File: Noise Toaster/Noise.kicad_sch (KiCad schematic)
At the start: 11 parts, among them Q5 2N3904, Q6 2N3904, Q7 2N3904

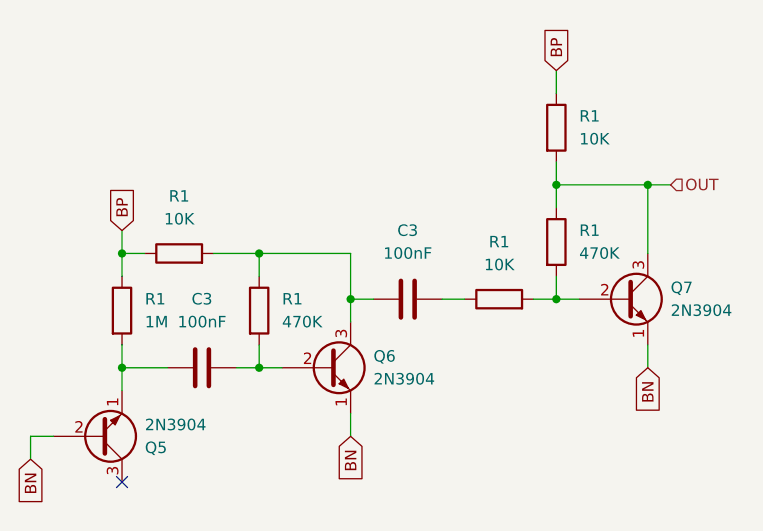
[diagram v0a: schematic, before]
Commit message: Noise Toaster - fixes after first board
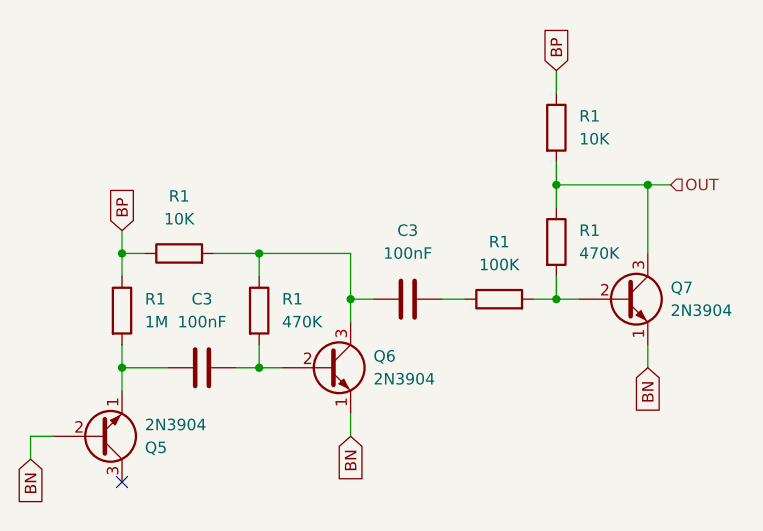
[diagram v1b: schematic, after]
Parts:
- R1: value 10K -> 100K
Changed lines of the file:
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@@
       (effects (font (size 1.27 1.27)))
     )
-    (property "Value" "10K" (at 160.02 92.71 90)
+    (property "Value" "100K" (at 160.02 92.71 90)
       (effects (font (size 1.27 1.27)))
     )

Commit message: misc
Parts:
- renumbered C3 to C15, C3 to C16, R1 to R33, R1 to R34, R1 to R35, R1 to R36, R1 to R37, R1 to R38
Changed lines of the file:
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@@
   (symbol (lib_id "Device:C") (at 149.86 96.52 270) (unit 1)
     (in_bom yes) (on_board yes) (dnp no) (fields_autoplaced)
-    (property "Reference" "C3" (at 149.86 88.9 90)
+    (property "Reference" "C16" (at 149.86 88.9 90)
       (effects (font (size 1.27 1.27)))
     )
@@
     (instances
       (project "Noise Toaster"
-        (path "/c06bdaff-9d92-4322-9a29-784b2d9ec2c6/3f36173e-f191-4036-853e-444de7299fbe"
-          (reference "C3") (unit 1)
-        )
         (path "/c06bdaff-9d92-4322-9a29-784b2d9ec2c6/059c9cca-6c24-4c13-86e8-c51a7e9129a9"
           (reference "C16") (unit 1)
@@
   (symbol (lib_id "Device:R") (at 118.11 97.79 0) (unit 1)
     (in_bom yes) (on_board yes) (dnp no) (fields_autoplaced)
-    (property "Reference" "R1" (at 120.65 96.52 0)
+    (property "Reference" "R33" (at 120.65 96.52 0)
       (effects (font (size 1.27 1.27)) (justify left))
     )
@@
     (instances
       (project "Noise Toaster"
-        (path "/c06bdaff-9d92-4322-9a29-784b2d9ec2c6/3f36173e-f191-4036-853e-444de7299fbe"
-          (reference "R1") (unit 1)
-        )
         (path "/c06bdaff-9d92-4322-9a29-784b2d9ec2c6/059c9cca-6c24-4c13-86e8-c51a7e9129a9"
           (reference "R33") (unit 1)
@@
   (symbol (lib_id "Device:R") (at 124.46 91.44 90) (unit 1)
     (in_bom yes) (on_board yes) (dnp no) (fields_autoplaced)
-    (property "Reference" "R1" (at 124.46 85.09 90)
+    (property "Reference" "R34" (at 124.46 85.09 90)
       (effects (font (size 1.27 1.27)))
     )
@@
     (instances
       (project "Noise Toaster"
-        (path "/c06bdaff-9d92-4322-9a29-784b2d9ec2c6/3f36173e-f191-4036-853e-444de7299fbe"
-          (reference "R1") (unit 1)
-        )
         (path "/c06bdaff-9d92-4322-9a29-784b2d9ec2c6/059c9cca-6c24-4c13-86e8-c51a7e9129a9"
           (reference "R34") (unit 1)
@@
   (symbol (lib_id "Device:R") (at 160.02 96.52 90) (unit 1)
     (in_bom yes) (on_board yes) (dnp no) (fields_autoplaced)
-    (property "Reference" "R1" (at 160.02 90.17 90)
+    (property "Reference" "R36" (at 160.02 90.17 90)
       (effects (font (size 1.27 1.27)))
     )
@@
     (instances
       (project "Noise Toaster"
-        (path "/c06bdaff-9d92-4322-9a29-784b2d9ec2c6/3f36173e-f191-4036-853e-444de7299fbe"
-          (reference "R1") (unit 1)
-        )
         (path "/c06bdaff-9d92-4322-9a29-784b2d9ec2c6/059c9cca-6c24-4c13-86e8-c51a7e9129a9"
           (reference "R36") (unit 1)
@@
   (symbol (lib_id "Device:R") (at 166.37 77.47 0) (unit 1)
     (in_bom yes) (on_board yes) (dnp no) (fields_autoplaced)
-    (property "Reference" "R1" (at 168.91 76.2 0)
+    (property "Reference" "R37" (at 168.91 76.2 0)
       (effects (font (size 1.27 1.27)) (justify left))
     )
@@
     (instances
       (project "Noise Toaster"
-        (path "/c06bdaff-9d92-4322-9a29-784b2d9ec2c6/3f36173e-f191-4036-853e-444de7299fbe"
-          (reference "R1") (unit 1)
-        )
         (path "/c06bdaff-9d92-4322-9a29-784b2d9ec2c6/059c9cca-6c24-4c13-86e8-c51a7e9129a9"
           (reference "R37") (unit 1)
@@
   (symbol (lib_id "Device:R") (at 133.35 97.79 0) (unit 1)
     (in_bom yes) (on_board yes) (dnp no) (fields_autoplaced)
-    (property "Reference" "R1" (at 135.89 96.52 0)
+    (property "Reference" "R35" (at 135.89 96.52 0)
       (effects (font (size 1.27 1.27)) (justify left))
     )
@@
     (instances
       (project "Noise Toaster"
-        (path "/c06bdaff-9d92-4322-9a29-784b2d9ec2c6/3f36173e-f191-4036-853e-444de7299fbe"
-          (reference "R1") (unit 1)
-        )
         (path "/c06bdaff-9d92-4322-9a29-784b2d9ec2c6/059c9cca-6c24-4c13-86e8-c51a7e9129a9"
           (reference "R35") (unit 1)
@@
   (symbol (lib_id "Device:C") (at 127 104.14 270) (unit 1)
     (in_bom yes) (on_board yes) (dnp no) (fields_autoplaced)
-    (property "Reference" "C3" (at 127 96.52 90)
+    (property "Reference" "C15" (at 127 96.52 90)
       (effects (font (size 1.27 1.27)))
     )
@@
     (instances
       (project "Noise Toaster"
-        (path "/c06bdaff-9d92-4322-9a29-784b2d9ec2c6/3f36173e-f191-4036-853e-444de7299fbe"
-          (reference "C3") (unit 1)
-        )
         (path "/c06bdaff-9d92-4322-9a29-784b2d9ec2c6/059c9cca-6c24-4c13-86e8-c51a7e9129a9"
           (reference "C15") (unit 1)
@@
   (symbol (lib_id "Device:R") (at 166.37 90.17 0) (unit 1)
     (in_bom yes) (on_board yes) (dnp no) (fields_autoplaced)
-    (property "Reference" "R1" (at 168.91 88.9 0)
+    (property "Reference" "R38" (at 168.91 88.9 0)
       (effects (font (size 1.27 1.27)) (justify left))
     )
@@
     (instances
       (project "Noise Toaster"
-        (path "/c06bdaff-9d92-4322-9a29-784b2d9ec2c6/3f36173e-f191-4036-853e-444de7299fbe"
-          (reference "R1") (unit 1)
-        )
         (path "/c06bdaff-9d92-4322-9a29-784b2d9ec2c6/059c9cca-6c24-4c13-86e8-c51a7e9129a9"
           (reference "R38") (unit 1)
